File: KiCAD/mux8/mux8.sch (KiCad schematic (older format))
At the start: 11 parts, among them P1 CONN_02X07, P2 CONN_02X07, U1 MAX14662, U2 MAX14662, U3 PCF8574

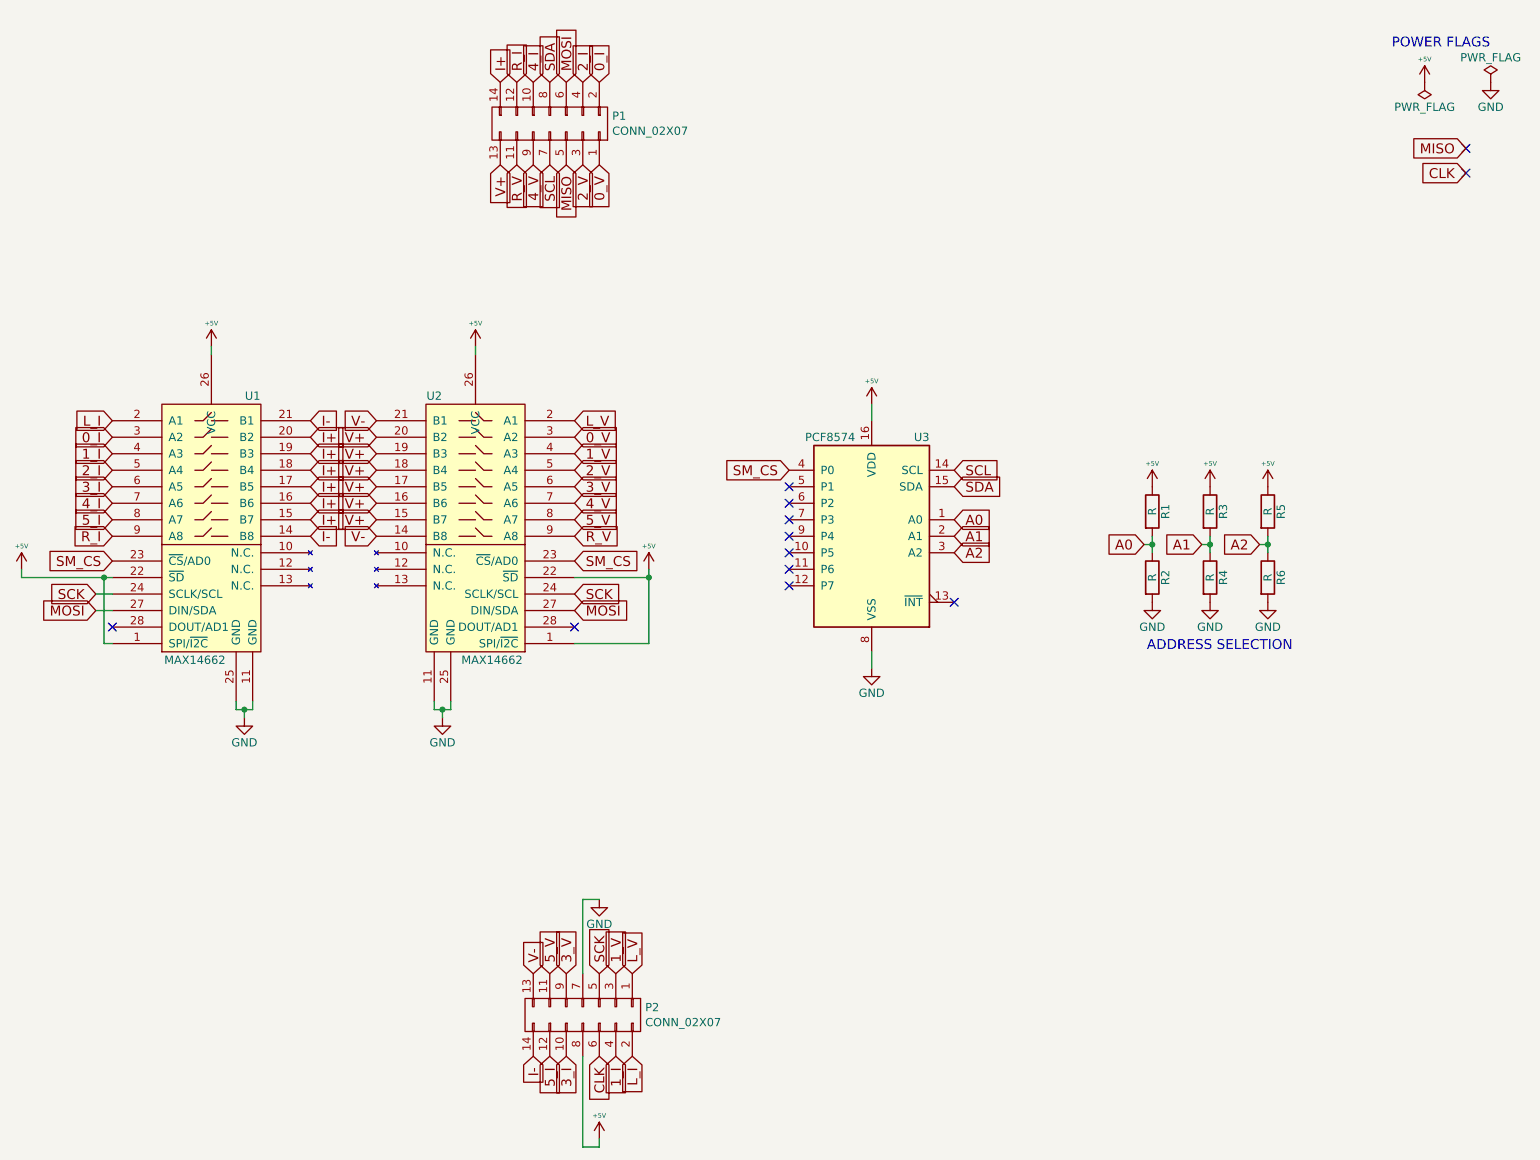
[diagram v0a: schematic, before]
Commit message: fix pwr/gnd swap, fix extra clock signal name, fix pin hole sizes
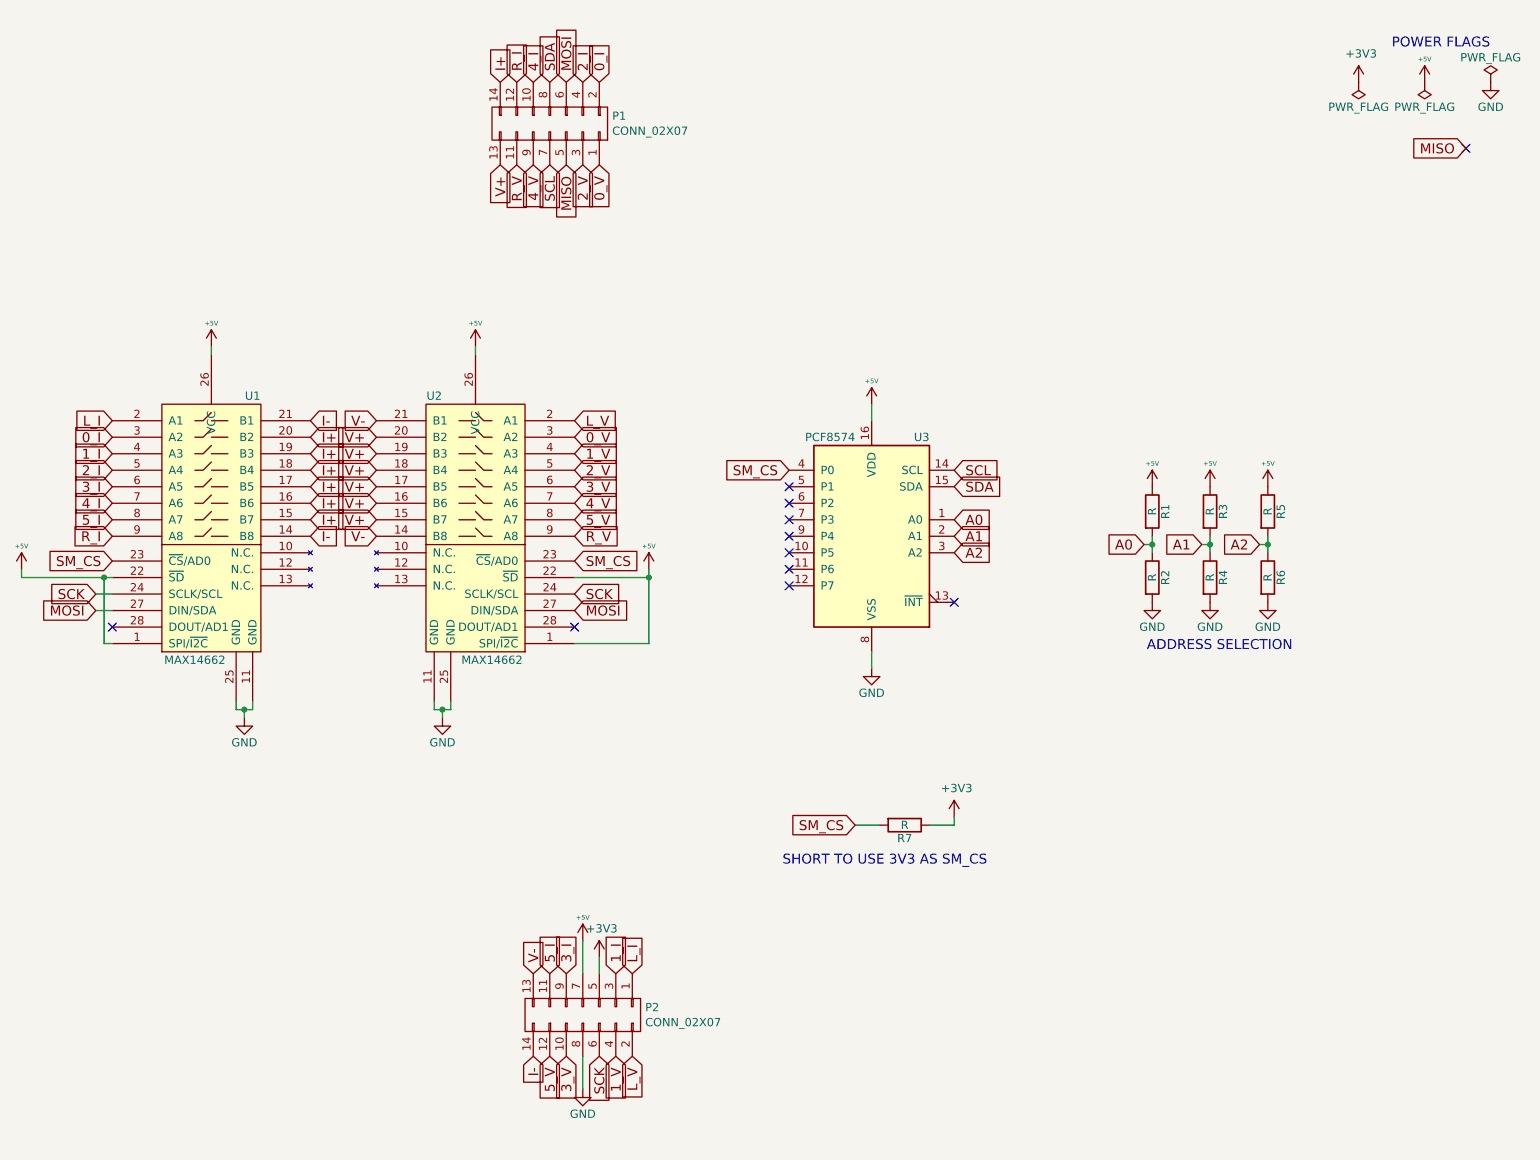
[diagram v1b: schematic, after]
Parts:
- added R7: R, Resistors_SMD:R_0402, symbol R
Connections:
- net CLK is gone; now on net SCK: P2.6 (P6)
- net +5V: now also P2.7 (P7); no longer P2.8 (P8)
- net 1_I: now also P2.3 (P3); no longer P2.4 (P4)
- net 1_V: now also P2.4 (P4); no longer P2.3 (P3)
- net 3_I: now also P2.9 (P9); no longer P2.10 (P10)
- net 3_V: now also P2.10 (P10); no longer P2.9 (P9)
- net 5_I: now also P2.11 (P11); no longer P2.12 (P12)
- net 5_V: now also P2.12 (P12); no longer P2.11 (P11)
- net GND: now also P2.8 (P8); no longer P2.7 (P7)
- net L_I: now also P2.1 (P1); no longer P2.2 (P2)
- net L_V: now also P2.2 (P2); no longer P2.1 (P1)
- net SCK: no longer P2.5 (P5)
- net SM_CS: now also R7.2
- new net +3V3: P2.5 (P5), R7.1
- no-connect marks 12 -> 11
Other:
- note added: "SHORT TO USE 3V3 AS SM_CS"
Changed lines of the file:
@@
 Text GLabel 5000 6300 1    60   Input ~ 0
 V-
+Text GLabel 5600 6800 3    60   Input ~ 0
+L_V
 Text GLabel 5600 6300 1    60   Input ~ 0
-L_V
-Text GLabel 5600 6800 3    60   Input ~ 0
 L_I
+Text GLabel 5500 6800 3    60   Input ~ 0
+1_V
 Text GLabel 5500 6300 1    60   Input ~ 0
-1_V
-Text GLabel 5500 6800 3    60   Input ~ 0
 1_I
-Text GLabel 5400 6300 1    60   Input ~ 0
+Text GLabel 5400 6800 3    60   Input ~ 0
 SCK
-Text GLabel 5400 6800 3    60   Input ~ 0
-CLK
+Text GLabel 5200 6800 3    60   Input ~ 0
+3_V
 Text GLabel 5200 6300 1    60   Input ~ 0
-3_V
-Text GLabel 5200 6800 3    60   Input ~ 0
 3_I
+Text GLabel 5100 6800 3    60   Input ~ 0
+5_V
 Text GLabel 5100 6300 1    60   Input ~ 0
-5_V
-Text GLabel 5100 6800 3    60   Input ~ 0
 5_I
 Text GLabel 5400 1400 3    60   Input ~ 0
@@
 $EndComp
 $Comp
-L GND #PWR01
+L GND #PWR11
 U 1 1 58FF94F7
 P 7050 4450
-F 0 "#PWR01" H 7050 4200 50  0001 C CNN
+F 0 "#PWR11" H 7050 4200 50  0001 C CNN
 F 1 "GND" H 7050 4300 50  0000 C CNN
 F 2 "" H 7050 4450 50  0000 C CNN
@@
 NoConn ~ 6550 3950
 $Comp
-L GND #PWR02
+L GND #PWR4
 U 1 1 58FF9502
 P 4450 4750
-F 0 "#PWR02" H 4450 4500 50  0001 C CNN
+F 0 "#PWR4" H 4450 4500 50  0001 C CNN
 F 1 "GND" H 4450 4600 50  0000 C CNN
 F 2 "" H 4450 4750 50  0000 C CNN
@@
 $EndComp
 $Comp
-L GND #PWR03
+L GND #PWR3
 U 1 1 58FF9508
 P 3250 4750
-F 0 "#PWR03" H 3250 4500 50  0001 C CNN
+F 0 "#PWR3" H 3250 4500 50  0001 C CNN
 F 1 "GND" H 3250 4600 50  0000 C CNN
 F 2 "" H 3250 4750 50  0000 C CNN
@@
 Text GLabel 4050 3550 0    60   Input ~ 0
 V+
-Text GLabel 6550 3250 0    60   Input ~ 0
+Text GLabel 6950 5400 0    60   Input ~ 0
 SM_CS
 Text GLabel 5250 3800 2    60   Input ~ 0
@@
 	1900 3850 1900 3900
 $Comp
-L +5V #PWR04
+L +5V #PWR2
 U 1 1 58FF955E
 P 3050 2500
-F 0 "#PWR04" H 3050 2350 50  0001 C CNN
+F 0 "#PWR2" H 3050 2350 50  0001 C CNN
 F 1 "+5V" H 3050 2640 28  0000 C CNN
 F 2 "" H 3050 2500 50  0000 C CNN
@@
 $EndComp
 $Comp
-L +5V #PWR05
+L +5V #PWR5
 U 1 1 58FF9564
 P 4650 2500
-F 0 "#PWR05" H 4650 2350 50  0001 C CNN
+F 0 "#PWR5" H 4650 2350 50  0001 C CNN
 F 1 "+5V" H 4650 2640 28  0000 C CNN
 F 2 "" H 4650 2500 50  0000 C CNN
@@
 $EndComp
 $Comp
-L +5V #PWR06
+L +5V #PWR10
 U 1 1 58FF956A
 P 7050 2850
-F 0 "#PWR06" H 7050 2700 50  0001 C CNN
+F 0 "#PWR10" H 7050 2700 50  0001 C CNN
 F 1 "+5V" H 7050 2990 28  0000 C CNN
 F 2 "" H 7050 2850 50  0000 C CNN
@@
 $EndComp
 $Comp
-L +5V #PWR07
+L +5V #PWR1
 U 1 1 58FF9570
 P 1900 3850
-F 0 "#PWR07" H 1900 3700 50  0001 C CNN
+F 0 "#PWR1" H 1900 3700 50  0001 C CNN
 F 1 "+5V" H 1900 3990 28  0000 C CNN
 F 2 "" H 1900 3850 50  0000 C CNN
@@
 $EndComp
 $Comp
-L +5V #PWR08
+L +5V #PWR9
 U 1 1 58FF9576
 P 5700 3850
-F 0 "#PWR08" H 5700 3700 50  0001 C CNN
+F 0 "#PWR9" H 5700 3700 50  0001 C CNN
 F 1 "+5V" H 5700 3990 28  0000 C CNN
 F 2 "" H 5700 3850 50  0000 C CNN
@@
 $EndComp
 $Comp
-L GND #PWR09
+L GND #PWR14
 U 1 1 58FF958D
 P 8750 4050
-F 0 "#PWR09" H 8750 3800 50  0001 C CNN
+F 0 "#PWR14" H 8750 3800 50  0001 C CNN
 F 1 "GND" H 8750 3900 50  0000 C CNN
 F 2 "" H 8750 4050 50  0000 C CNN
@@
 $EndComp
 $Comp
-L +5V #PWR010
+L +5V #PWR13
 U 1 1 58FF9593
 P 8750 3350
-F 0 "#PWR010" H 8750 3200 50  0001 C CNN
+F 0 "#PWR13" H 8750 3200 50  0001 C CNN
 F 1 "+5V" H 8750 3490 28  0000 C CNN
 F 2 "" H 8750 3350 50  0000 C CNN
@@
 $EndComp
 $Comp
-L GND #PWR011
+L GND #PWR16
 U 1 1 58FF95AE
 P 9100 4050
-F 0 "#PWR011" H 9100 3800 50  0001 C CNN
+F 0 "#PWR16" H 9100 3800 50  0001 C CNN
 F 1 "GND" H 9100 3900 50  0000 C CNN
 F 2 "" H 9100 4050 50  0000 C CNN
@@
 $EndComp
 $Comp
-L +5V #PWR012
+L +5V #PWR15
 U 1 1 58FF95B4
 P 9100 3350
-F 0 "#PWR012" H 9100 3200 50  0001 C CNN
+F 0 "#PWR15" H 9100 3200 50  0001 C CNN
 F 1 "+5V" H 9100 3490 28  0000 C CNN
 F 2 "" H 9100 3350 50  0000 C CNN
@@
 $EndComp
 $Comp
-L GND #PWR013
+L GND #PWR18
 U 1 1 58FF95CC
 P 9450 4050
-F 0 "#PWR013" H 9450 3800 50  0001 C CNN
+F 0 "#PWR18" H 9450 3800 50  0001 C CNN
 F 1 "GND" H 9450 3900 50  0000 C CNN
 F 2 "" H 9450 4050 50  0000 C CNN
@@
 $EndComp
 $Comp
-L +5V #PWR014
+L +5V #PWR17
 U 1 1 58FF95D2
 P 9450 3350
-F 0 "#PWR014" H 9450 3200 50  0001 C CNN
+F 0 "#PWR17" H 9450 3200 50  0001 C CNN
 F 1 "+5V" H 9450 3490 28  0000 C CNN
 F 2 "" H 9450 3350 50  0000 C CNN
@@
 SM_CS
 $Comp
-L GND #PWR015
+L GND #PWR21
 U 1 1 58FF8E6A
 P 10800 900
-F 0 "#PWR015" H 10800 650 50  0001 C CNN
+F 0 "#PWR21" H 10800 650 50  0001 C CNN
 F 1 "GND" H 10800 750 50  0000 C CNN
 F 2 "" H 10800 900 50  0000 C CNN
@@
 $EndComp
 $Comp
-L +5V #PWR016
+L +5V #PWR20
 U 1 1 58FF8E76
 P 10400 900
-F 0 "#PWR016" H 10400 750 50  0001 C CNN
+F 0 "#PWR20" H 10400 750 50  0001 C CNN
 F 1 "+5V" H 10400 1040 28  0000 C CNN
 F 2 "" H 10400 900 50  0000 C CNN
@@
 $EndComp
 $Comp
-L PWR_FLAG #FLG017
+L PWR_FLAG #FLG2
 U 1 1 58FF8E7C
 P 10400 900
-F 0 "#FLG017" H 10400 975 50  0001 C CNN
+F 0 "#FLG2" H 10400 975 50  0001 C CNN
 F 1 "PWR_FLAG" H 10400 1050 50  0000 C CNN
 F 2 "" H 10400 900 50  0000 C CNN
@@
 $EndComp
 $Comp
-L PWR_FLAG #FLG018
+L PWR_FLAG #FLG3
 U 1 1 58FF8E88
 P 10800 900
-F 0 "#FLG018" H 10800 975 50  0001 C CNN
+F 0 "#FLG3" H 10800 975 50  0001 C CNN
 F 1 "PWR_FLAG" H 10800 1050 50  0000 C CNN
 F 2 "" H 10800 900 50  0000 C CNN
@@
 POWER FLAGS
 $Comp
-L GND #PWR019
+L GND #PWR7
 U 1 1 58FF923B
-P 5400 5850
-F 0 "#PWR019" H 5400 5600 50  0001 C CNN
-F 1 "GND" H 5400 5700 50  0000 C CNN
-F 2 "" H 5400 5850 50  0000 C CNN
-F 3 "" H 5400 5850 50  0000 C CNN
-	1    5400 5850
-	-1   0    0    -1
-$EndComp
-$Comp
-L +5V #PWR020
+P 5300 7000
+F 0 "#PWR7" H 5300 6750 50  0001 C CNN
+F 1 "GND" H 5300 6850 50  0000 C CNN
+F 2 "" H 5300 7000 50  0000 C CNN
+F 3 "" H 5300 7000 50  0000 C CNN
+	1    5300 7000
+	-1   0    0    -1
+$EndComp
+$Comp
+L +5V #PWR6
 U 1 1 58FF9319
-P 5400 7300
-F 0 "#PWR020" H 5400 7150 50  0001 C CNN
-F 1 "+5V" H 5400 7440 28  0000 C CNN
-F 2 "" H 5400 7300 50  0000 C CNN
-F 3 "" H 5400 7300 50  0000 C CNN
-	1    5400 7300
+P 5300 6100
+F 0 "#PWR6" H 5300 5950 50  0001 C CNN
+F 1 "+5V" H 5300 6240 28  0000 C CNN
+F 2 "" H 5300 6100 50  0000 C CNN
+F 3 "" H 5300 6100 50  0000 C CNN
+	1    5300 6100
 	1    0    0    -1
 $EndComp
@@
 Text GLabel 5100 900  1    60   Input ~ 0
 SDA
-Wire Wire Line
-	5400 5850 5300 5850
-Wire Wire Line
-	5300 5850 5300 6300
-Wire Wire Line
-	5300 6800 5300 7350
-Wire Wire Line
-	5300 7350 5400 7350
-Wire Wire Line
-	5400 7350 5400 7300
-Text GLabel 10650 1450 0    60   Input ~ 0
-CLK
 NoConn ~ 10650 1300
-NoConn ~ 10650 1450
 Text GLabel 10650 1300 0    60   Input ~ 0
 MISO
+$Comp
+L R R7
+U 1 1 5927D2E3
+P 7250 5400
+F 0 "R7" V 7330 5400 50  0000 C CNN
+F 1 "R" V 7250 5400 50  0000 C CNN
+F 2 "Resistors_SMD:R_0402" V 7180 5400 50  0001 C CNN
+F 3 "" H 7250 5400 50  0000 C CNN
+	1    7250 5400
+	0    1    1    0
+$EndComp
+Wire Wire Line
+	5300 6800 5300 7000
+Wire Wire Line
+	5300 6300 5300 6100
+$Comp
+L PWR_FLAG #FLG1
+U 1 1 5927DD86
+P 10000 900
+F 0 "#FLG1" H 10000 975 50  0001 C CNN
+F 1 "PWR_FLAG" H 10000 1050 50  0000 C CNN
+F 2 "" H 10000 900 50  0000 C CNN
+F 3 "" H 10000 900 50  0000 C CNN
+	1    10000 900
+	-1   0    0    1
+$EndComp
+Wire Wire Line
+	6950 5400 7100 5400
+Text Notes 7750 5650 2    60   ~ 0
+SHORT TO USE 3V3 AS SM_CS
+Text GLabel 6550 3250 0    60   Input ~ 0
+SM_CS
+$Comp
+L +3V3 #PWR19
+U 1 1 5927E199
+P 10000 900
+F 0 "#PWR19" H 10000 750 50  0001 C CNN
+F 1 "+3V3" H 10015 1073 50  0000 C CNN
+F 2 "" H 10000 900 50  0001 C CNN
+F 3 "" H 10000 900 50  0001 C CNN
+	1    10000 900
+	1    0    0    -1
+$EndComp
+$Comp
+L +3V3 #PWR8
+U 1 1 5927E247
+P 5400 6200
+F 0 "#PWR8" H 5400 6050 50  0001 C CNN
+F 1 "+3V3" H 5415 6373 50  0000 C CNN
+F 2 "" H 5400 6200 50  0001 C CNN
+F 3 "" H 5400 6200 50  0001 C CNN
+	1    5400 6200
+	1    0    0    -1
+$EndComp
+Wire Wire Line
+	5400 6300 5400 6200
+$Comp
+L +3V3 #PWR12
+U 1 1 5927E4EB
+P 7550 5350
+F 0 "#PWR12" H 7550 5200 50  0001 C CNN
+F 1 "+3V3" H 7565 5523 50  0000 C CNN
+F 2 "" H 7550 5350 50  0001 C CNN
+F 3 "" H 7550 5350 50  0001 C CNN
+	1    7550 5350
+	1    0    0    -1
+$EndComp
+Wire Wire Line
+	7400 5400 7550 5400
+Wire Wire Line
+	7550 5400 7550 5350
 $EndSCHEMATC
